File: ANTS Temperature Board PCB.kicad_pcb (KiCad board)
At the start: 2 copper layers, 50 x 80 mm, 16 parts, among them J1 1751251, J2 1751251, J3 EBWA-02-A, J4 EBWA-02-A, J5 EBWA-02-A, J6 B2B-XH-A, J7 B2B-XH-A, Q1 IRLZ34N, Q2 IRLZ34N, U1 RASPBERRY_PI_PICO

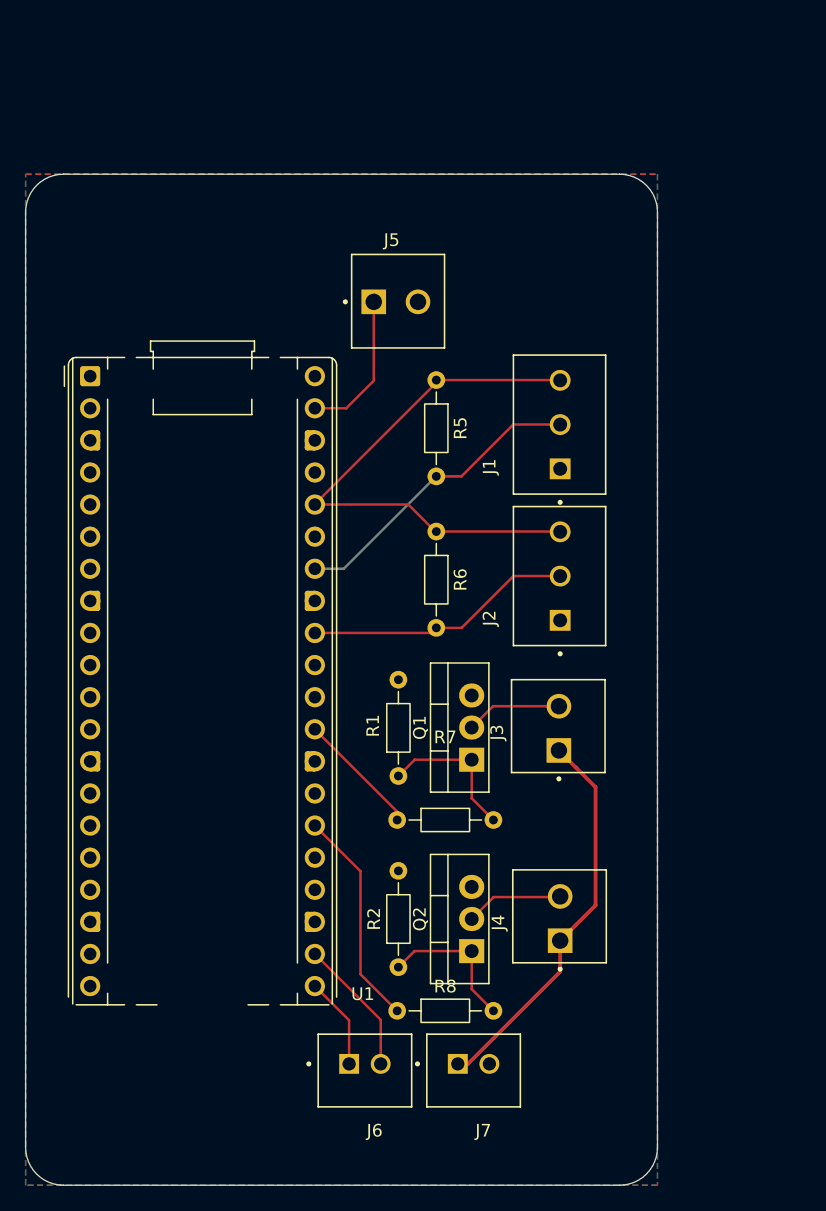
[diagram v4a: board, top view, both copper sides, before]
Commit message: Added Mounting Holes
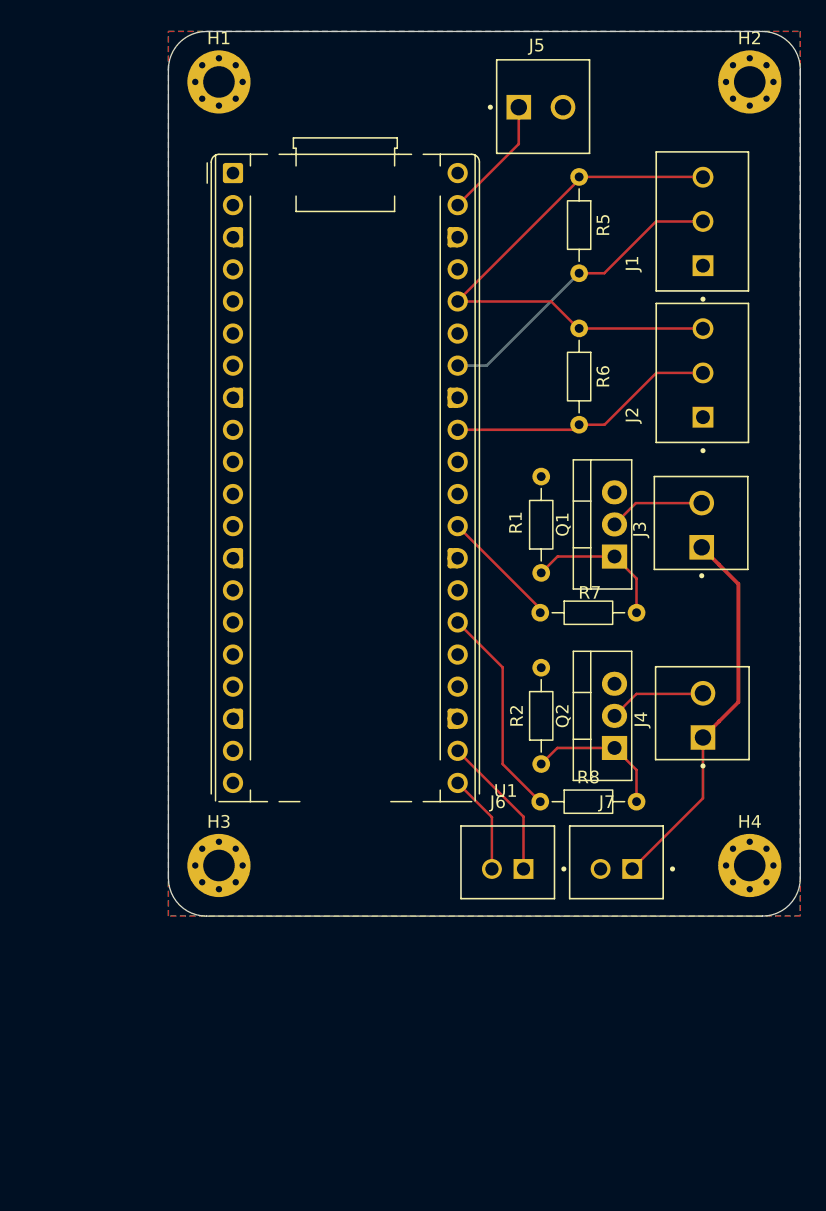
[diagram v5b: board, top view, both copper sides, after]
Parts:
- added H1: MountingHole_Pad, MountingHole:MountingHole_2.5mm_Pad_Via, F.Cu at (72.3, 30.7)
- added H2: MountingHole_Pad, MountingHole:MountingHole_2.5mm_Pad_Via, F.Cu at (114.3, 30.7)
- added H3: MountingHole_Pad, MountingHole:MountingHole_2.5mm_Pad_Via, F.Cu at (72.3, 92.7)
- added H4: MountingHole_Pad, MountingHole:MountingHole_2.5mm_Pad_Via, F.Cu at (114.3, 92.7)
- moved R8 20.1 mm to (97.7, 87.7)
- moved J6 20.0 mm to (95.2, 92.5), turned to 0 degrees
- moved J7 20.0 mm to (103.8, 92.5), turned to 0 degrees
- moved R7 19.9 mm to (97.7, 72.7)
- moved R1 19.6 mm to (97.8, 69.5)
- moved R2 19.6 mm to (97.8, 84.7)
- moved R6 19.6 mm to (100.8, 50.2)
- moved U1 19.6 mm to (73.4, 37.9)
- moved J3 19.6 mm to (110.5, 65.8)
- moved J4 19.6 mm to (110.6, 80.8)
- moved Q1 19.6 mm to (103.6, 68.3)
- moved Q2 19.6 mm to (103.6, 83.4)
- moved R5 19.6 mm to (100.8, 38.2)
- moved J1 19.6 mm to (114.2, 47.2)
- moved J2 19.6 mm to (114.2, 59.2)
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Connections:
- U1 pad 21: /UART_RX -> /UART_TX
- U1 pad 22: /UART_TX -> /UART_RX
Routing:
- net /UART_RX: track 7.28 -> 11.5 mm
- net /UART_TX: track 10.9 -> 7.93 mm
- net /VSYS: track 11.8 -> 9.75 mm
- net +7.5V: track 31.0 -> 30.1 mm
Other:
- board size 50 x 80 mm -> 50 x 70 mm

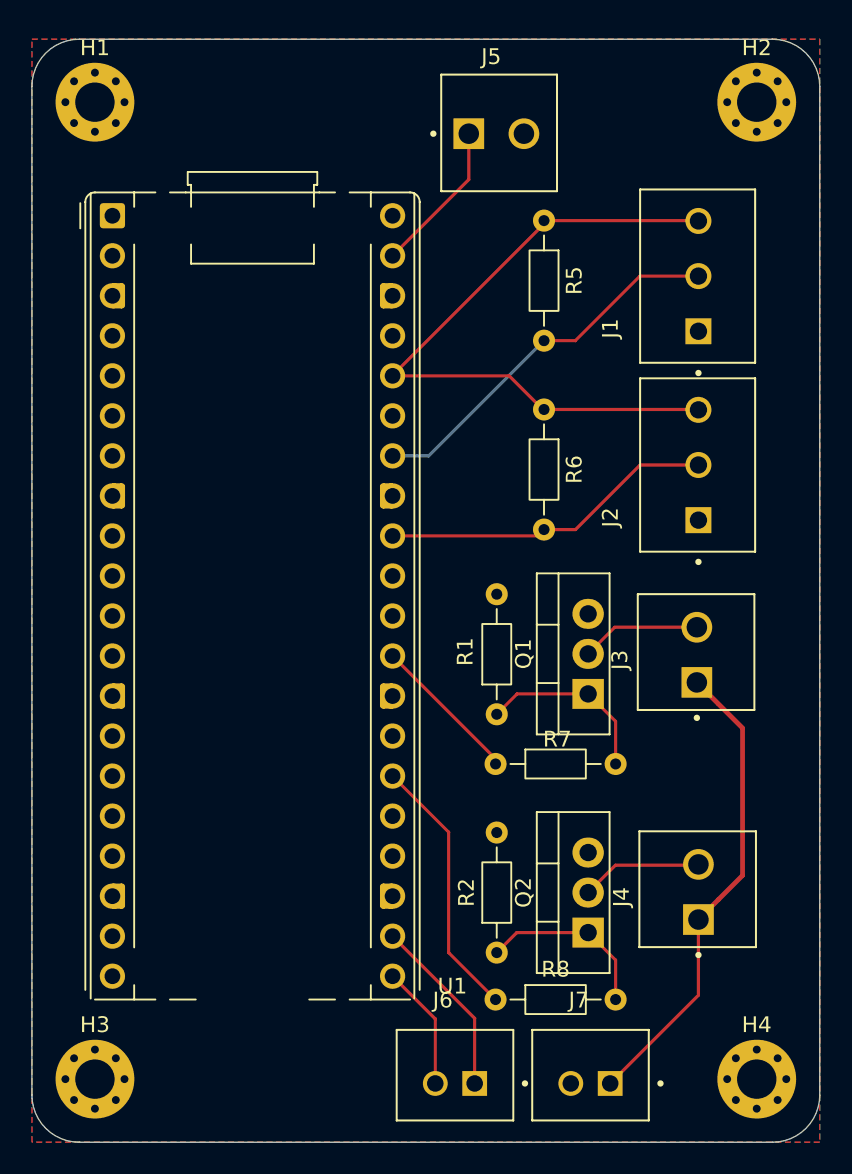
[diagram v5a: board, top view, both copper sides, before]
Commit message: Changed layout a bit to prevent wiring overlap.
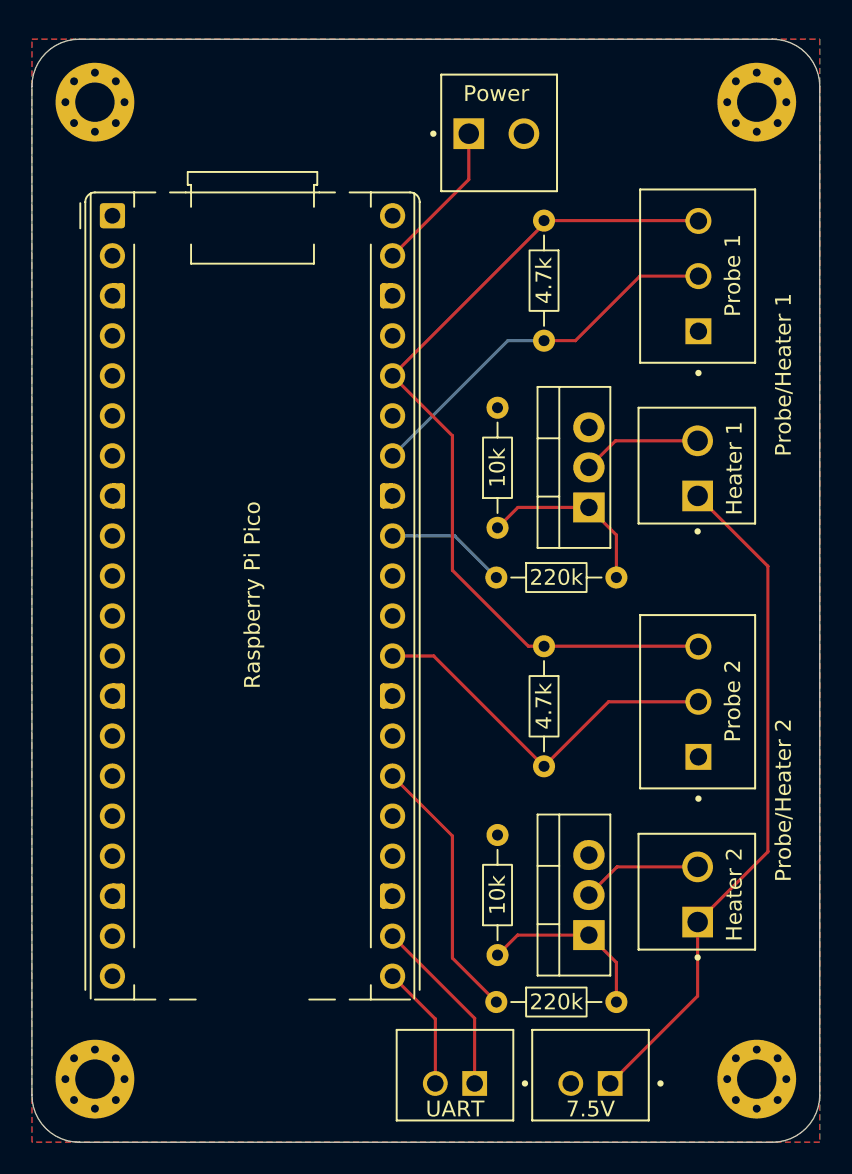
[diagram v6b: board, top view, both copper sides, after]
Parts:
- moved R6 15.0 mm to (100.8, 65.2)
- moved J2 15.0 mm to (114.2, 74.2)
- moved J3 11.8 mm to (110.5, 53.9)
- moved Q1 11.8 mm to (103.7, 56.4)
- moved R7 11.8 mm to (97.8, 60.9)
- moved R1 11.8 mm to (97.8, 57.7)
- moved J4 0.16 mm to (110.5, 81.0)
- moved Q2 0.16 mm to (103.7, 83.6)
- moved R2 0.16 mm to (97.8, 84.8)
- moved R8 0.16 mm to (97.8, 87.8)
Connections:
- U1 pad 29: /mosfet1_gate -> /SIGNAL2
- U1 pad 32: /SIGNAL2 -> /mosfet1_gate
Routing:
- net +7.5V: track 30.1 -> 43.3 mm
- net +3V3: track 43.9 -> 55.2 mm
- net /SIGNAL2: track 21.3 -> 24.0 mm
- net /mosfet1_gate: track 9.56 -> 7.68 mm
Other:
- board text added: "10k"
- board text added: "220k"
- board text added: "4.7k"
- board text added: "7.5V"
- board text added: "Heater 1"
- board text added: "Heater 2"
- board text added: "Power"
- board text added: "Probe 1"
- board text added: "Probe 2"
- board text added: "Probe/Heater 1"
- board text added: "Probe/Heater 2"
- board text added: "Raspberry Pi Pico"
- board text added: "UART"

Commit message: Adding silkscreens
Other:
- board text added: "IRLZ34N"
- board text added: "Left-TX Right-RX"
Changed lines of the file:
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@@
 		)
 		(property "Value" "IRLZ34N"
-			(at 2.54 2.2 90)
+			(at 2.54 -1.88 90)
 			(layer "F.Fab")
 			(effects
@@
 		)
 		(property "Value" "B2B-XH-A"
-			(at 3.67 4.76 0)
+			(at -0.000825 -1.51 0)
 			(layer "F.Fab")
 			(effects
@@
 		)
 		(property "Value" "IRLZ34N"
-			(at 2.54 2.2 90)
+			(at 2.54 -1.88 90)
 			(layer "F.Fab")
 			(effects
@@
 		)
 		(property "Value" "B2B-XH-A"
-			(at 3.67 4.76 0)
+			(at -0.000825 -1.51 0)
 			(layer "F.Fab")
 			(effects
@@
 		)
 	)
+	(gr_text "Left-TX\nRight-RX"
+		(at 90.77 92.45 0)
+		(layer "F.SilkS")
+		(effects
+			(font
+				(size 1 1)
+				(thickness 0.1)
+			)
+			(justify right)
+		)
+	)
 	(gr_text "Raspberry Pi Pico"
 		(at 82.300825 61.98 90)
@@
 		(layer "F.SilkS")
 		(effects
+			(font
+				(size 1 1)
+				(thickness 0.1)
+			)
+		)
+	)
+	(gr_text "IRLZ34N"
+		(at 101.77 53.88 90)
+		(layer "F.SilkS")
+		(effects
+			(font
+				(size 1 1)
+				(thickness 0.1)
+			)
+		)
+	)
+	(gr_text "IRLZ34N"
+		(at 101.77 81.0175 90)
+		(layer "F.SilkS")
+		(effects

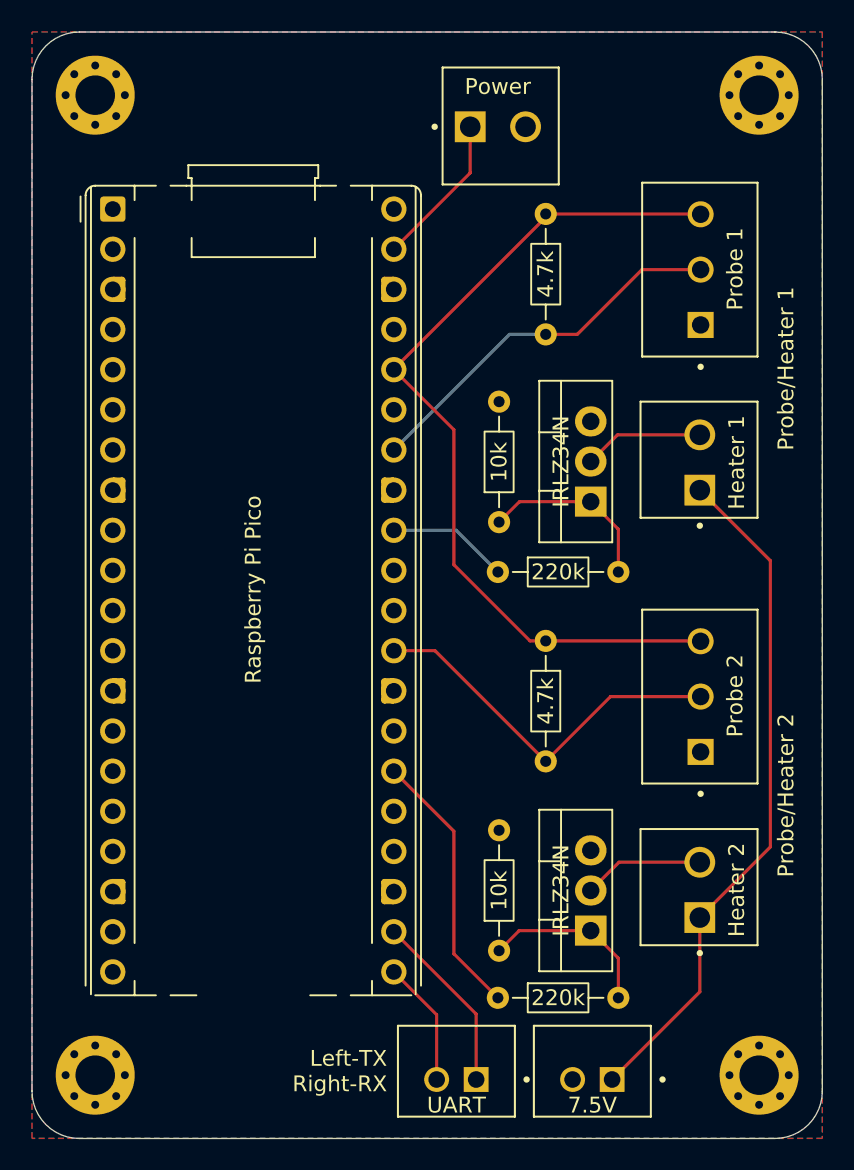
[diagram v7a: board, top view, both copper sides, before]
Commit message: deleted one probe and one heater, changed mounting hole footprint to 2.5m holes, and organized board. Also updated schematic.
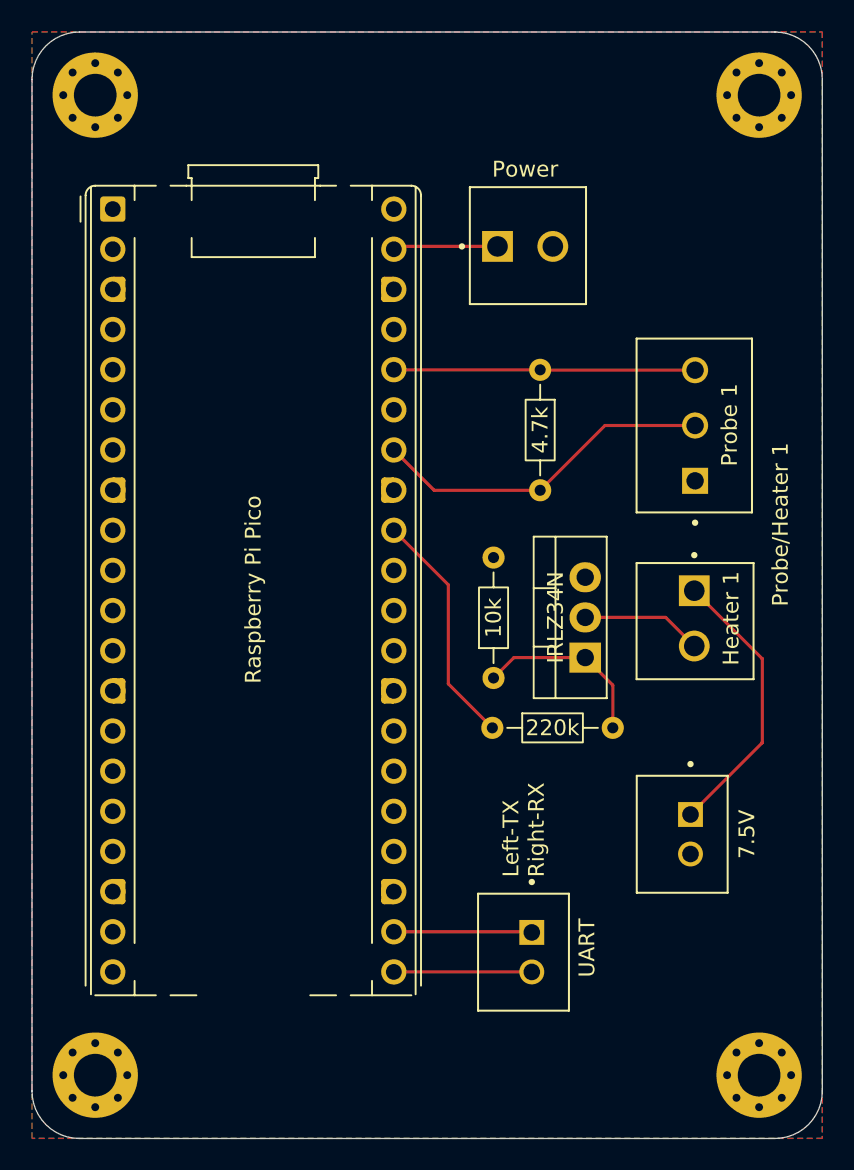
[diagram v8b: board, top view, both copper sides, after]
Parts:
- removed J2: 1751251, 67TERM BLOCK:PHOENIX_1751251
- removed J4: EBWA-02-A, 2 PIN TERM:ADAMTECH_EBWA-02-A
- removed Q2: IRLZ34N, Package_TO_SOT_THT:TO-220-3_Vertical
- removed R2: 10k, Resistor_THT:R_Axial_DIN0204_L3.6mm_D1.6mm_P7.62mm_Horizontal
- removed R6: 4.7K, Resistor_THT:R_Axial_DIN0204_L3.6mm_D1.6mm_P7.62mm_Horizontal
- removed R8: 220, Resistor_THT:R_Axial_DIN0204_L3.6mm_D1.6mm_P7.62mm_Horizontal
- H1, H2, H3, H4: footprint MountingHole:MountingHole_2.5mm_Pad_Via -> MountingHole:MountingHole_2.7mm_M2.5_Pad_Via
- moved J7 16.0 mm to (109.4, 77.5), turned to 90 degrees
- moved J3 9.87 mm to (110.2, 63.8), turned to -90 degrees
- moved Q1 9.87 mm to (103.3, 66.3)
- moved R7 9.87 mm to (97.4, 70.7)
- moved J1 9.87 mm to (113.8, 57.1)
- moved R1 9.87 mm to (97.5, 67.6)
- moved R5 9.87 mm to (100.5, 48.1)
- moved J6 8.64 mm to (99.4, 84.9), turned to 90 degrees
- moved J5 7.76 mm to (99.5, 40.3)
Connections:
- U1 pad 26: /mosfet2_gate -> unconnected-(U1-GP20-Pad26)
- U1 pad 29: /SIGNAL2 -> unconnected-(U1-GP22-Pad29)
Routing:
- net +3V3: track 55.2 -> 19.1 mm
- net +7.5V: track 43.3 -> 17.8 mm
- net /SIGNAL2: track 24.0 -> 0.00 mm
- net /mosfet2_gate: track 17.1 -> 0.00 mm
- net Net-(Q2-G): track 11.3 -> 0.00 mm
- net Net-(J4-Drain): track 7.64 -> 0.00 mm
- net /mosfet1_gate: track 7.68 -> 15.1 mm
- net /VSYS: track 9.75 -> 6.63 mm
- net /UART_RX: track 11.5 -> 8.75 mm
- net /SIGNAL1: track 24.1 -> 21.8 mm
- net /UART_TX: track 7.93 -> 8.73 mm
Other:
- board text removed: "Heater 2"
- board text removed: "Probe 2"
- board text removed: "Probe/Heater 2"
